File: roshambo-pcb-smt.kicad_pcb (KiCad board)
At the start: 2 copper layers, 49 parts, among them J1 Conn_01x06_Socket, J2 Conn_01x03_Pin, J3 Conn_01x03_Pin, Q1 2N7002, Q2 2N7002, Q3 2N7002, Q4 2N7002, Q5 2N7002, Q6 2N7002, Q7 2N7002, Q8 2N7002, Q9 2N7002, U1 Pico

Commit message: start layout
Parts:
- moved J2 75.0 mm to (111.8, 109.2)
- moved J3 73.3 mm to (147.3, 109.2)
- moved Q3 59.0 mm to (52.1, 49.9)
- moved Q2 55.0 mm to (52.1, 45.4)
- moved Q1 50.9 mm to (52.1, 41.0)
- moved D3 39.7 mm to (119.4, 58.9)
- moved D2 38.0 mm to (119.4, 50.8)
- moved D1 35.8 mm to (119.4, 43.2)
- moved J1 34.4 mm to (111.8, 72.4)
- moved D7 34.0 mm to (143.8, 43.2)
- moved D4 31.6 mm to (132.1, 43.2)
- moved D8 30.1 mm to (143.8, 50.8)
- moved D5 29.5 mm to (132.1, 50.8)
- moved R10 29.3 mm to (39.6, 45.0)
- moved R11 29.3 mm to (39.6, 47.5)
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
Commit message: More progress on the layout
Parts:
- D1, D2, D3, D4, D5, D6, D7, D8, D9: footprint LED_SMD:LED_0805_2012Metric -> LED_SMD:LED_0603_1608Metric
- R1, R10, R11, R12, R13, R14, R15, R16, R17, R18, R19, R2, R20, R21, R22, R23, R24, R25, R26, R27, R3, R4, R5, R6, R7, R8, R9: footprint Resistor_SMD:R_0603_1608Metric -> Resistor_SMD:R_0402_1005Metric
- moved R19 91.3 mm to (133.8, 35.6), turned to 90 degrees
- moved R20 90.7 mm to (133.8, 43.2), turned to 90 degrees
- moved R21 90.3 mm to (133.8, 50.8), turned to 90 degrees
- moved R12 80.4 mm to (120.0, 50.8), turned to 90 degrees
- moved R10 80.3 mm to (119.4, 35.4), turned to 90 degrees
- moved R11 79.9 mm to (119.4, 42.9), turned to 90 degrees
- moved R25 78.9 mm to (125.9, 37.2), turned to -90 degrees
- moved R22 78.4 mm to (125.9, 34.3), turned to 90 degrees
- moved R24 78.3 mm to (125.9, 49.7), turned to 90 degrees
- moved R27 78.3 mm to (126.0, 52.6), turned to -90 degrees
- moved R26 77.9 mm to (125.3, 44.6), turned to -90 degrees
- moved R23 77.7 mm to (125.4, 41.7), turned to 90 degrees
- moved R13 75.2 mm to (112.6, 34.4), turned to 90 degrees
- moved R14 74.2 mm to (112.6, 42.0), turned to 90 degrees
- moved R3 71.9 mm to (107.3, 50.8), turned to 90 degrees
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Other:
- board outline added: 50 x 80 mm

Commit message: Released to Production
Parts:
- D1, D4, D7: value LED -> RED
- D2, D5, D9: value LED -> GREEN
- D3, D6: value LED -> BLUE
- D8: value LED -> YELLOW
- R1, R10, R19, R20: value 47 -> 150
- R11, R2, R21: value 47 -> 40
- R12, R3: value 47 -> 88
- moved U1 1.83 mm to (118.5, 80.3)
- moved J2 1.83 mm to (100.7, 98.1)
- moved J3 1.83 mm to (136.2, 98.1)
- moved J1 1.83 mm to (100.7, 61.3)
- moved R19 1.32 mm to (132.7, 35.0)
- moved R20 1.32 mm to (132.7, 42.6)
- moved R21 1.32 mm to (132.7, 50.2)
- moved D7 1.32 mm to (135.8, 34.8)
- moved D8 1.32 mm to (135.8, 42.5)
- moved D9 1.32 mm to (135.8, 50.6)
- moved R16 0.66 mm to (112.4, 36.4), turned to -90 degrees
- moved R17 0.66 mm to (112.5, 44.1)
- moved R18 0.66 mm to (112.6, 52.0)
- moved R23 0.66 mm to (125.1, 41.1)
- moved R6 0.66 mm to (99.7, 48.5)
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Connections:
- Q9 pad 1: GND -> Net-(Q9-G)
- R24 pad 2: GND -> Net-(Q9-G)
- R27 pad 1: GND -> Net-(Q9-G)
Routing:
- net +5V: track 0.00 -> 93.2 mm
- net /TX1: track 0.00 -> 92.1 mm
- net /RX1: track 0.00 -> 83.9 mm
- net /PWM1A: track 0.00 -> 83.5 mm
- net /PWM1B: track 0.00 -> 73.4 mm
- net /PWM2A: track 0.00 -> 62.9 mm
- net /PWM2B: track 0.00 -> 62.2 mm
- net /PWM4A: track 0.00 -> 54.6 mm, vias 0 -> 1
- net /PWM4B: track 0.00 -> 49.0 mm, vias 0 -> 1
- net /PWM5A: track 0.00 -> 46.3 mm, vias 0 -> 1
- net /PWM3A: track 0.00 -> 38.8 mm, vias 0 -> 1
- net /PWM3B: track 0.00 -> 33.1 mm, vias 0 -> 1
- net Net-(Q2-G): track 0.00 -> 7.46 mm
- net Net-(Q1-G): track 0.00 -> 7.38 mm
- net Net-(Q3-G): track 0.00 -> 6.90 mm
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- added copper zone on B.Cu, net GND
- added copper zone on F.Cu, net GND
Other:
- board size 50 x 80 mm -> 43 x 78.5 mm

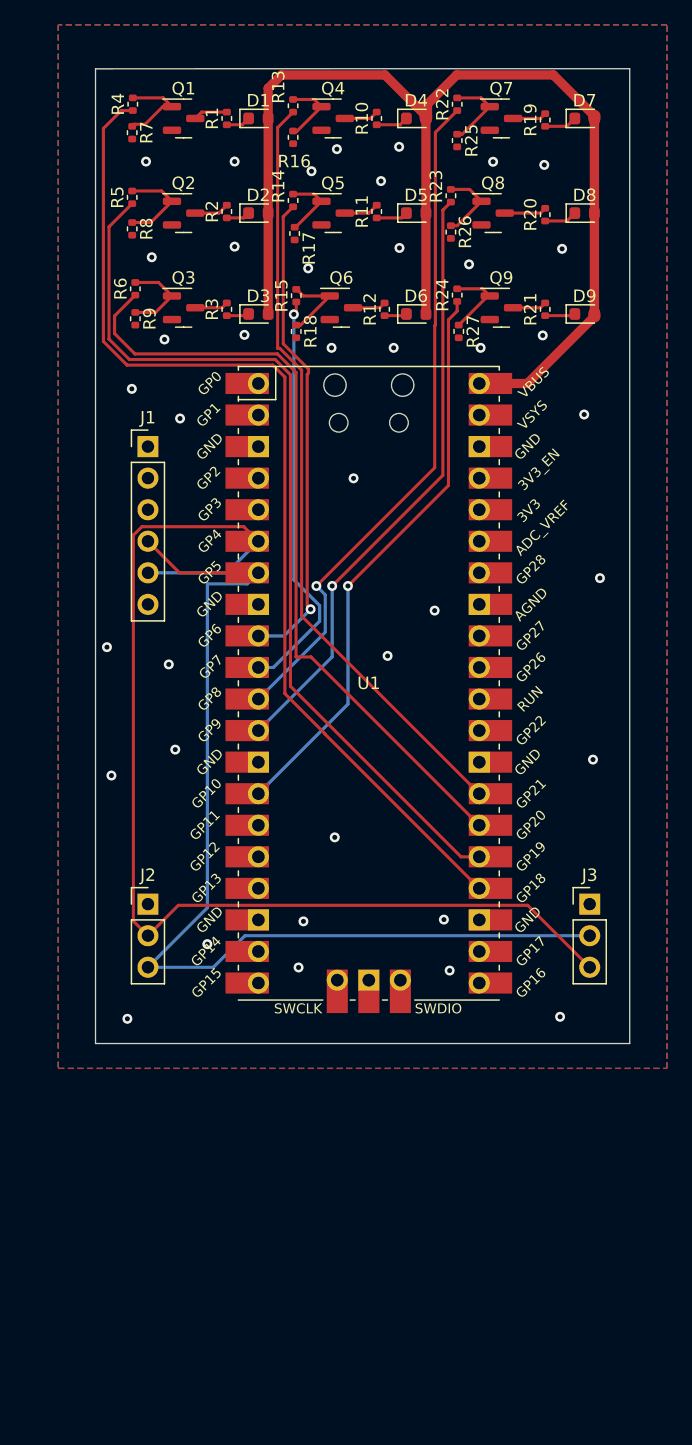
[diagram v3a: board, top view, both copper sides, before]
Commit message: use 595 shift registers
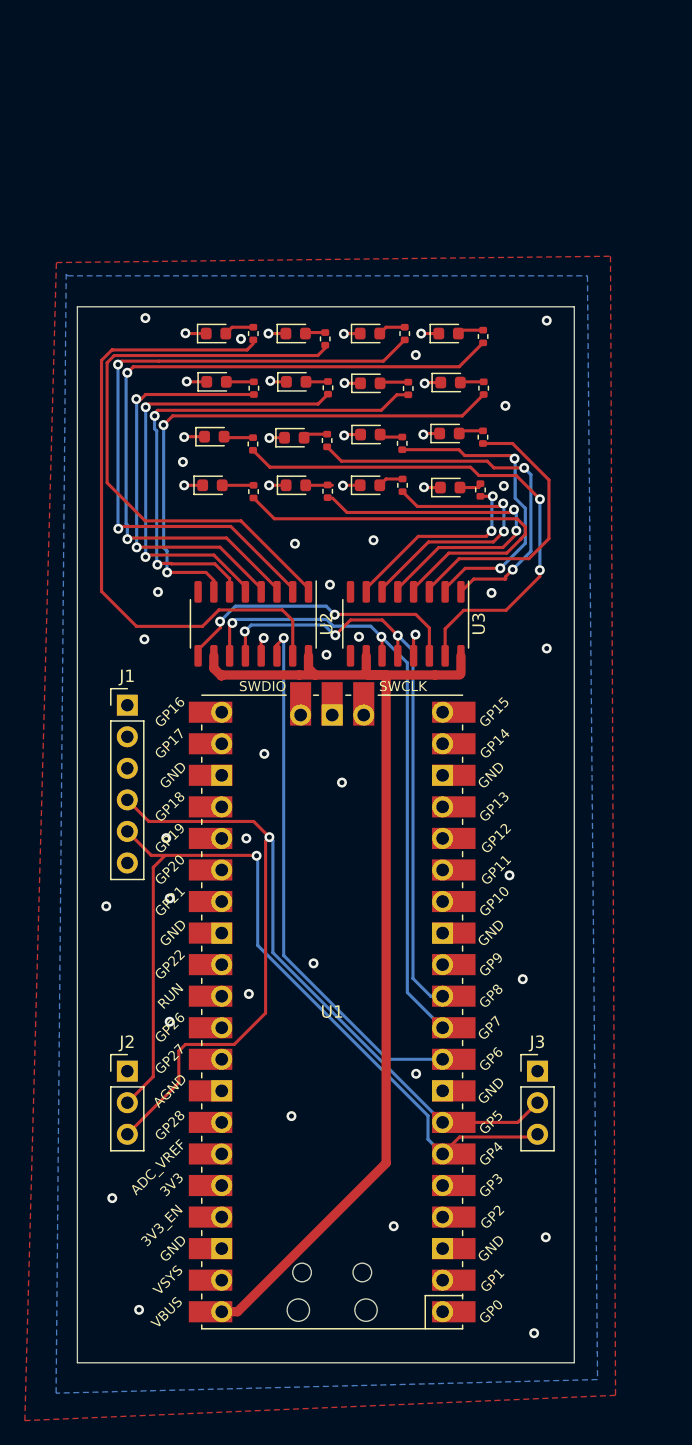
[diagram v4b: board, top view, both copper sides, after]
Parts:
- removed Q1, Q2, Q3, Q4, Q5, Q6, Q7, Q8, Q9: 2N7002, Package_TO_SOT_SMD:SOT-23
- removed R17, R18, R25, R26, R27: 1.1M, Resistor_SMD:R_0402_1005Metric
- removed R19, R20: 150, Resistor_SMD:R_0402_1005Metric
- removed R21: 40, Resistor_SMD:R_0402_1005Metric
- removed R22, R23, R24: 100, Resistor_SMD:R_0402_1005Metric
- added D10: GREEN, LED_SMD:LED_0603_1608Metric, F.Cu at (112.5, 60.5)
- added D11: BLUE, LED_SMD:LED_0603_1608Metric, F.Cu at (118.6, 60.3)
- added D12: YELLOW, LED_SMD:LED_0603_1608Metric, F.Cu at (124.9, 60.2)
- added D13: RED, LED_SMD:LED_0603_1608Metric, F.Cu at (105.9, 64.4)
- added D14: GREEN, LED_SMD:LED_0603_1608Metric, F.Cu at (112.6, 64.4)
- added D15: BLUE, LED_SMD:LED_0603_1608Metric, F.Cu at (118.6, 64.4)
- added D16: YELLOW, LED_SMD:LED_0603_1608Metric, F.Cu at (125.0, 64.5)
- added U2: 74HC595, Package_SO:SO-16_3.9x9.9mm_P1.27mm, F.Cu at (109.2, 75.5)
- added U3: 74HC595, Package_SO:SO-16_3.9x9.9mm_P1.27mm, F.Cu at (121.4, 75.5)
- D4: value RED -> YELLOW
- D5, D9: value GREEN -> RED
- D6: value BLUE -> GREEN
- D7: value RED -> BLUE
- R10: value 150 -> 40
- R11: value 40 -> 88
- R12: value 88 -> 150
- R13, R4, R5: value 100 -> 150
- R14, R6: value 100 -> 40
- R15: value 100 -> 88
- R16, R8, R9: value 1.1M -> 150
- R7: value 1.1M -> 88
- moved R4 33.8 mm to (127.7, 52.4)
- moved R16 32.1 mm to (127.4, 64.7), turned to 90 degrees
- moved D9 31.4 mm to (106.0, 60.5)
- moved R13 31.2 mm to (109.2, 64.9)
- moved R8 31.1 mm to (127.7, 56.5), turned to 90 degrees
- moved R7 30.3 mm to (121.6, 56.6), turned to 90 degrees
- moved D7 27.4 mm to (118.6, 56.2)
- moved U1 26.6 mm to (115.5, 106.8), turned to 180 degrees
- moved R10 26.2 mm to (115.1, 60.8)
- moved R14 23.6 mm to (115.1, 64.8)
- moved D5 21.0 mm to (106.2, 56.0)
- moved J1 20.9 mm to (99.0, 82.1)
- moved R11 18.8 mm to (121.1, 61.0)
- moved R5 18.2 mm to (109.2, 56.5)
- moved D1 17.6 mm to (106.2, 52.2)
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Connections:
- D1 pad 1: Net-(D1-K) -> GND
- D1 pad 2: +5V -> Net-(D1-A)
- D2 pad 1: Net-(D2-K) -> GND
- D2 pad 2: +5V -> Net-(D2-A)
- D3 pad 1: Net-(D3-K) -> GND
- D3 pad 2: +5V -> Net-(D3-A)
- D4 pad 1: Net-(D4-K) -> GND
- D4 pad 2: +5V -> Net-(D4-A)
- D5 pad 1: Net-(D5-K) -> GND
- D5 pad 2: +5V -> Net-(D5-A)
- D6 pad 1: Net-(D6-K) -> GND
- D6 pad 2: +5V -> Net-(D6-A)
- D7 pad 1: Net-(D7-K) -> GND
- D7 pad 2: +5V -> Net-(D7-A)
- D8 pad 1: Net-(D8-K) -> GND
- D8 pad 2: +5V -> Net-(D8-A)
- D9 pad 1: Net-(D9-K) -> GND
- D9 pad 2: +5V -> Net-(D9-A)
- R1 pad 1: Net-(D1-K) -> /D1
- R1 pad 2: Net-(Q1-D) -> Net-(D1-A)
- R10 pad 1: Net-(D4-K) -> /D10
- R11 pad 1: Net-(D5-K) -> /D11
- R12 pad 1: Net-(D6-K) -> /D12
- R13 pad 1: /PWM2B -> /D13
- R13 pad 2: Net-(Q4-G) -> Net-(D13-A)
- R14 pad 1: /PWM3A -> /D14
- R15 pad 1: /PWM3B -> /D15
- R16 pad 1: Net-(Q4-G) -> /D16
- R16 pad 2: GND -> Net-(D16-A)
- R2 pad 1: Net-(D2-K) -> /D2
- R2 pad 2: Net-(Q2-D) -> Net-(D2-A)
- R3 pad 1: Net-(D3-K) -> /D3
- R3 pad 2: Net-(Q3-D) -> Net-(D3-A)
- R4 pad 1: /PWM1A -> /D4
- R4 pad 2: Net-(Q1-G) -> Net-(D4-A)
- R5 pad 1: /PWM1B -> /D5
- R5 pad 2: Net-(Q2-G) -> Net-(D5-A)
- R6 pad 1: /PWM2A -> /D6
- R6 pad 2: Net-(Q3-G) -> Net-(D6-A)
- R7 pad 1: Net-(Q1-G) -> /D7
- R7 pad 2: GND -> Net-(D7-A)
- R8 pad 1: Net-(Q2-G) -> /D8
- R8 pad 2: GND -> Net-(D8-A)
- R9 pad 1: Net-(Q3-G) -> /D9
- R9 pad 2: GND -> Net-(D9-A)
- U1 pad 10: /PWM3B -> /SRCLK
- U1 pad 11: /PWM4A -> /RCLK
- U1 pad 12: /PWM4B -> unconnected-(U1-GPIO9-Pad12)
- U1 pad 13: GND -> unconnected-(U1-GND-Pad13)
- U1 pad 14: /PWM5A -> unconnected-(U1-GPIO10-Pad14)
- U1 pad 15: /PWM5B -> unconnected-(U1-GPIO11-Pad15)
- U1 pad 24: /PWM1A -> unconnected-(U1-GPIO18-Pad24)
- U1 pad 25: /PWM1B -> unconnected-(U1-GPIO19-Pad25)
- U1 pad 26: /PWM2A -> unconnected-(U1-GPIO20-Pad26)
- U1 pad 27: /PWM2B -> unconnected-(U1-GPIO21-Pad27)
- U1 pad 9: /PWM3A -> /SER
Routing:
- net /PWM1A: track 83.5 -> 0.00 mm
- net /PWM1B: track 73.4 -> 0.00 mm
- net /PWM2A: track 62.9 -> 0.00 mm
- net /PWM2B: track 62.2 -> 0.00 mm
- net /D4: track 0.00 -> 57.2 mm, vias 0 -> 2
- net /PWM4A: track 54.6 -> 0.00 mm, vias 1 -> 0
- net /D3: track 0.00 -> 53.6 mm, vias 0 -> 2
- net /D1: track 0.00 -> 51.7 mm
- net /SRCLK: track 0.00 -> 50.5 mm, vias 0 -> 2
- net /PWM4B: track 49.0 -> 0.00 mm, vias 1 -> 0
- net /RCLK: track 0.00 -> 48.6 mm, vias 0 -> 3
- net /D2: track 0.00 -> 48.0 mm
- net /PWM5A: track 46.3 -> 0.00 mm, vias 1 -> 0
- net /D8: track 0.00 -> 43.7 mm, vias 0 -> 2
- net /SER: track 0.00 -> 43.5 mm, vias 0 -> 1
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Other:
- board size 43 x 78.5 mm -> 40 x 85 mm

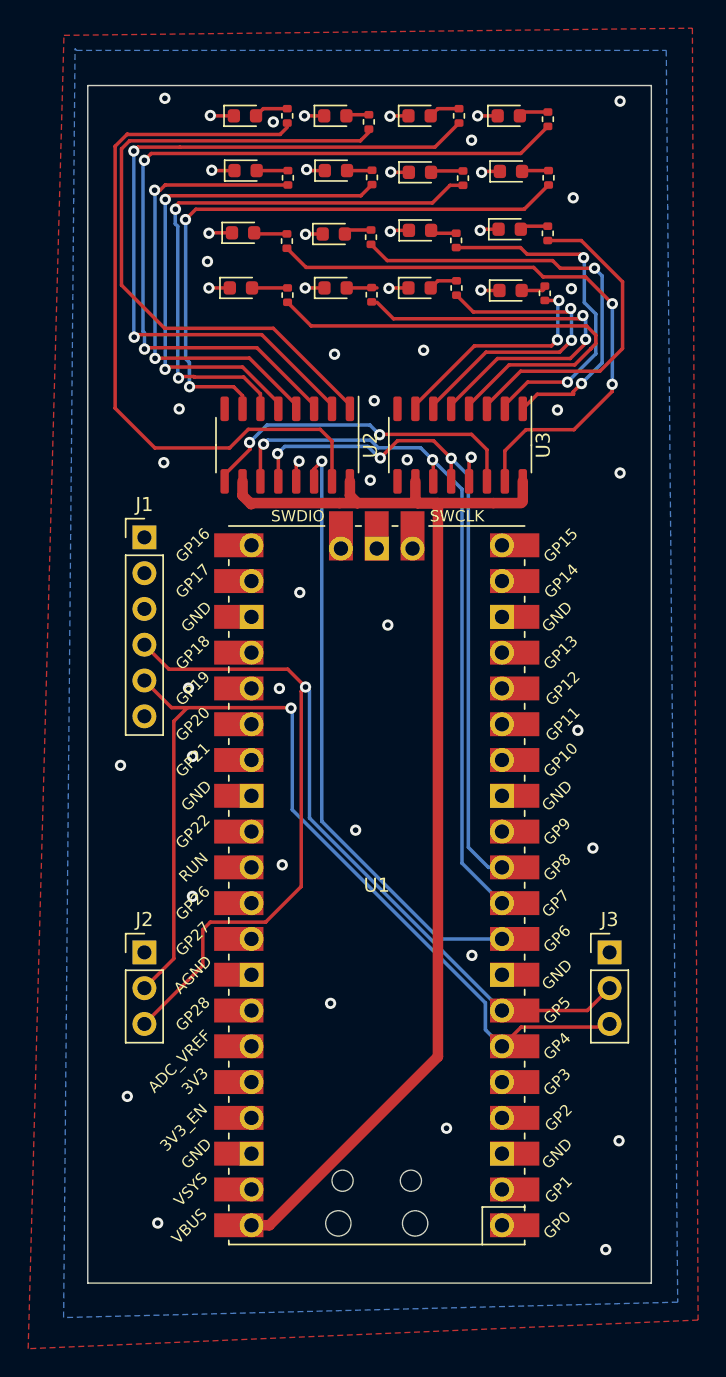
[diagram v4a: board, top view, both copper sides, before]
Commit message: Add reset switch, OE
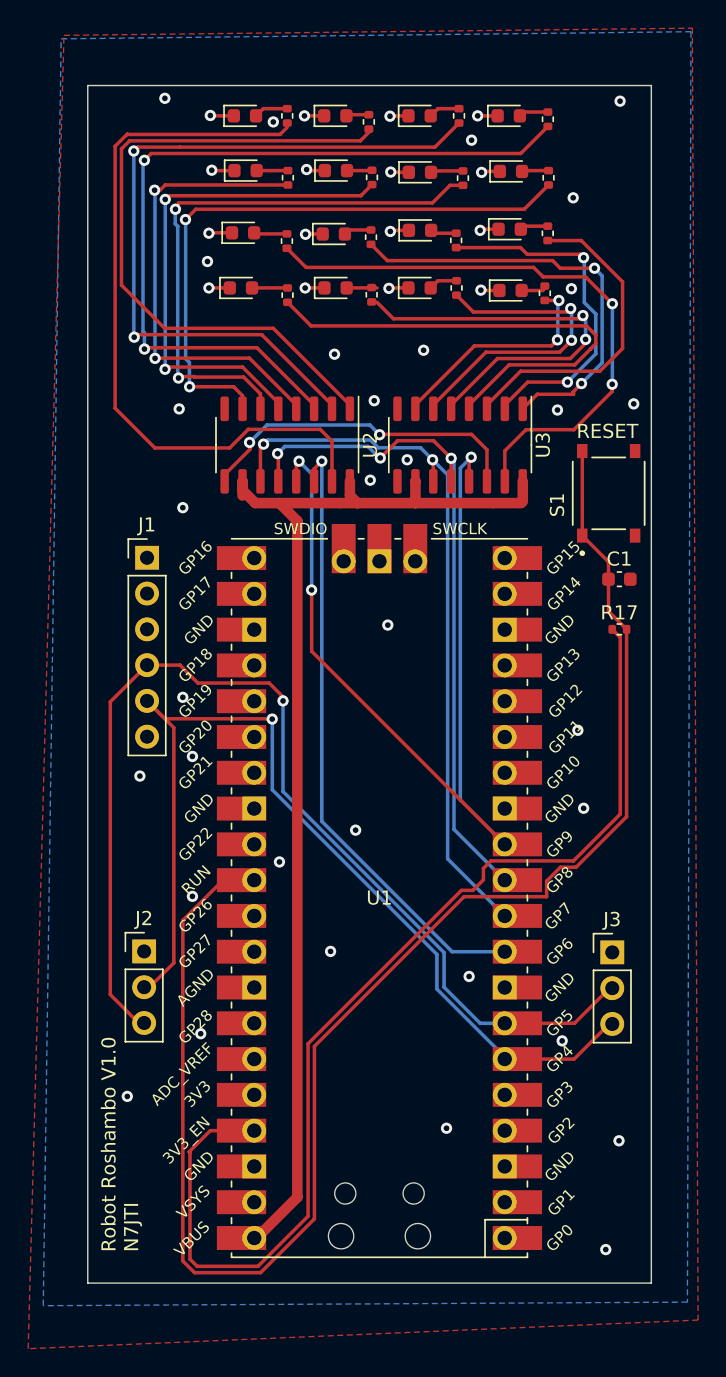
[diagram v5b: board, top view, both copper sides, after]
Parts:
- added C1: 1uF, Capacitor_SMD:C_0603_1608Metric, F.Cu at (132.7, 85.0)
- added R17: 10k, Resistor_SMD:R_0402_1005Metric, F.Cu at (132.7, 88.6)
- added S1: TS-1187A-B-A-B, TS-1187A-B-A-B:SW_TS-1187A-B-A-B, F.Cu at (132.0, 78.9)
- moved J1 1.46 mm to (99.2, 83.5)
- moved U1 0.93 mm to (115.7, 107.7)
- moved J3 0.19 mm to (132.2, 111.5)
- moved J2 0.07 mm to (99.0, 111.5)
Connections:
- U1 pad 12: unconnected-(U1-GPIO9-Pad12) -> /OE
- U1 pad 30: unconnected-(U1-RUN-Pad30) -> Net-(U1-RUN)
- U1 pad 37: unconnected-(U1-3V3_EN-Pad37) -> Net-(U1-3V3_EN)
- U2 pad 13: GND -> /OE
- U3 pad 13: GND -> /OE
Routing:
- net Net-(U1-RUN): track 0.00 -> 110.7 mm
- net Net-(U1-3V3_EN): track 0.00 -> 77.9 mm
- net /OE: track 0.00 -> 65.6 mm, vias 0 -> 3
- net +5V: track 85.0 -> 80.7 mm
- net GND: track 25.9 -> 22.6 mm, vias 52 -> 49
- net /RX1: track 80.7 -> 77.6 mm
- net /SRCLK: track 50.5 -> 51.5 mm
- net /SER: track 43.5 -> 44.0 mm
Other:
- board text added: "RESET"
- board text added: "Robot Roshambo V1.0 N7JTI"
